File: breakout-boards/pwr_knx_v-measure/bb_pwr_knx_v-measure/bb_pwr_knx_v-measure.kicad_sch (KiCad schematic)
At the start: 47 parts, among them IC100 BD9G101, T1 BC856, T2 BCP52, T3 BC847

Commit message: bump bb_pwr_knx_v WIP
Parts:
- removed JP3: PINHD-1X2, bb_pwr_knx_v-measure:1X02, symbol bb_pwr_knx_v-measure-eagle-import:PINHD-1X2
- added C7: 100n, Capacitor_SMD:C_0805_2012Metric, symbol Device:C
- added D8: 1N4148W, Diode_SMD:D_SOD-123, symbol Diode:1N4148W
- added R14: 390k, Resistor_SMD:R_0805_2012Metric, symbol Device:R
- added R15: 43k, Resistor_SMD:R_0805_2012Metric, symbol Device:R
- C1: value 100uF 35V -> 100µ/35V; footprint bb_pwr_knx_v-measure:SANYO-OSCON_SMD_C6 -> Capacitor_SMD:CP_Elec_6.3x7.7; symbol bb_pwr_knx_v-measure-eagle-import:CPOL-EUSANYO_SMD_C6 -> Device:C_Polarized
- C10, C104, C2, C6: value 100nF -> 100n; footprint bb_pwr_knx_v-measure:C0805 -> Capacitor_SMD:C_0805_2012Metric; symbol bb_pwr_knx_v-measure-eagle-import:C-EUC0805 -> Device:C
- C100: value 4.7uF 50V -> 4.7µ/35V; footprint bb_pwr_knx_v-measure:C0805 -> Capacitor_SMD:C_0805_2012Metric; symbol bb_pwr_knx_v-measure-eagle-import:C-EUC0805 -> Device:C; REICHELT X7R-G1206 4,7/50 -> (none)
- C101: value 470nF -> 270n; footprint bb_pwr_knx_v-measure:C0805 -> Capacitor_SMD:C_0805_2012Metric; symbol bb_pwr_knx_v-measure-eagle-import:C-EUC0805 -> Device:C; now not fitted
- C102: value 15nF -> 15n; footprint bb_pwr_knx_v-measure:C0805 -> Capacitor_SMD:C_0805_2012Metric; symbol bb_pwr_knx_v-measure-eagle-import:C-EUC0805 -> Device:C; REICHELT X7R-G0805 15N -> (none)
- C103, C105: value 47uF 10V -> 47µ/10V; footprint bb_pwr_knx_v-measure:C0805 -> Capacitor_SMD:C_1206_3216Metric; symbol bb_pwr_knx_v-measure-eagle-import:C-EUC0805 -> Device:C
- C3, C4: value 10nF -> 10n; footprint bb_pwr_knx_v-measure:C0805 -> Capacitor_SMD:C_0805_2012Metric; symbol bb_pwr_knx_v-measure-eagle-import:C-EUC0805 -> Device:C
- C5: value 100pF -> 100p; footprint bb_pwr_knx_v-measure:C0805 -> Capacitor_SMD:C_0805_2012Metric; symbol bb_pwr_knx_v-measure-eagle-import:C-EUC0805 -> Device:C
- D1: value SMAJCA -> SMAJ40CA; footprint bb_pwr_knx_v-measure:DO214AC -> Diode_SMD:D_SMA; symbol bb_pwr_knx_v-measure-eagle-import:SMAJCA -> Diode:SMAJ40CA
- D100: value MBRS1100 -> RB060M-60 / MBR 140SFT1G; footprint bb_pwr_knx_v-measure:SOD-123 -> Diode_SMD:D_SOD-123; symbol bb_pwr_knx_v-measure-eagle-import:DIODESOD-123 -> Device:D_Schottky
- D2, D3, D4, D5: value 1N4148 -> 1N4148W; footprint bb_pwr_knx_v-measure:SOD-123 -> Diode_SMD:D_SOD-123; symbol bb_pwr_knx_v-measure-eagle-import:DIODESOD-123 -> Diode:1N4148W
- D6: footprint bb_pwr_knx_v-measure:SOD-123 -> Diode_SMD:D_SOD-123; symbol bb_pwr_knx_v-measure-eagle-import:DIODESOD-123 -> Device:D_Zener
- D7: value DDZ9685 -> 3V6; footprint bb_pwr_knx_v-measure:SOD-123 -> Diode_SMD:D_SOD-123; symbol bb_pwr_knx_v-measure-eagle-import:DIODESOD-123 -> Device:D_Zener
- IC100: value BD9G101 -> TPS560430; footprint bb_pwr_knx_v-measure:SOT23-6 -> Package_TO_SOT_SMD:SOT-23-6; symbol bb_pwr_knx_v-measure-eagle-import:BD9G101GBD9G101G-SOT23-6 -> Regulator_Switching:MCP16331x-xCH
- JP2: value PINHD-1X3 -> Conn_01x03_Pin; footprint bb_pwr_knx_v-measure:1X03 -> Connector_PinHeader_2.54mm:PinHeader_1x05_P2.54mm_Vertical; symbol bb_pwr_knx_v-measure-eagle-import:PINHD-1X3 -> Connector:Conn_01x05_Pin
- JP4: value PINHD-1X2 -> Conn_01x02_Pin; footprint bb_pwr_knx_v-measure:1X02 -> Connector_PinHeader_2.54mm:PinHeader_1x02_P2.54mm_Vertical; symbol bb_pwr_knx_v-measure-eagle-import:PINHD-1X2 -> Connector:Conn_01x02_Pin
- KNX0: footprint bb_pwr_knx_v-measure:WAGO-243-211 -> selfbus:W243-211_1x02_P5.75; symbol bb_pwr_knx_v-measure-eagle-import:WAGO-243-211 -> Connector:Screw_Terminal_01x02
- L1: footprint bb_pwr_knx_v-measure:BS11 -> selfbus:BS11_LIEGEND; SPICEPREFIX L -> (none)
- L100: value 4.7uH -> 10u; footprint bb_pwr_knx_v-measure:L4532P -> Inductor_SMD:L_1812_4532Metric; symbol bb_pwr_knx_v-measure-eagle-import:L-EUL4532P -> Device:L
- R1, R10, R11, R12, R13, R2, R3, R4, R5, R7, R8, R9: footprint bb_pwr_knx_v-measure:R0805 -> Resistor_SMD:R_0805_2012Metric; symbol bb_pwr_knx_v-measure-eagle-import:R-EU_R0805 -> Device:R
- R101: value 1k6 -> 88k7; footprint bb_pwr_knx_v-measure:R0805 -> Resistor_SMD:R_0805_2012Metric; symbol bb_pwr_knx_v-measure-eagle-import:R-EU_R0805 -> Device:R
- R102: value 470R -> 22k1; footprint bb_pwr_knx_v-measure:R0805 -> Resistor_SMD:R_0805_2012Metric; symbol bb_pwr_knx_v-measure-eagle-import:R-EU_R0805 -> Device:R
- R25: value 24R 2512 1.0W -> 24R 1W; footprint bb_pwr_knx_v-measure:R2512 -> Resistor_SMD:R_1206_3216Metric; symbol bb_pwr_knx_v-measure-eagle-import:R-EU_R2512 -> Device:R
- R6: footprint bb_pwr_knx_v-measure:R0805 -> Resistor_SMD:R_0805_2012Metric; symbol bb_pwr_knx_v-measure-eagle-import:R-EU_R0805 -> Device:R; REICHELT SMD-0805 5,60K -> (none)
- T1: footprint bb_pwr_knx_v-measure:SOT23-BEC -> Package_TO_SOT_SMD:SOT-23; symbol bb_pwr_knx_v-measure-eagle-import:BC856SMD -> Transistor_BJT:BC856
- T2: value BCP52 -> FZT753; footprint bb_pwr_knx_v-measure:SOT223 -> Package_TO_SOT_SMD:SOT-223-3_TabPin2; symbol bb_pwr_knx_v-measure-eagle-import:FZT753SMD -> Device:Q_PNP_BCE
- T3: footprint bb_pwr_knx_v-measure:SOT23 -> Package_TO_SOT_SMD:SOT-23; symbol bb_pwr_knx_v-measure-eagle-import:BC847 -> Transistor_BJT:BC847; REICHELT BC 847C SMD -> (none)
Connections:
- net +3V3: now also JP2.2 (Pin_2), D8.2 (A)
- net BUS_V: now also D7.1 (K), JP2.4 (Pin_4); no longer D7.C, JP2.2
- net EIB+: now also D1.2 (A2), D2.2 (A), D3.2 (A), KNX0.2 (Pin_2); no longer D1.C (2), D2.A, D3.A, KNX0.1+
- net EIB+DIR: now also D2.1 (K); no longer D2.C
- net EIB_DC: now also C1.1, D6.1 (K), C7.1, R14.2; no longer C1.+, D4.C, D6.C, IC100.4 (EN)
- net EIB_IN: now also C6.1, T1.2 (E); no longer T1.E
- net EIB_OUT: now also JP2.5 (Pin_5); no longer JP2.1
- net GND: now also C1.2, D1.1 (A1), D100.2 (A), D4.2 (A), D7.2 (A), JP2.1 (Pin_1), KNX0.1 (Pin_1), T1.3 (C), C7.2, R15.1; no longer C1.-, C6.1, D1.A (1), D100.A, D7.A, KNX0.2-, T1.C
- net N$8: no longer T2.4 (C)
- net REF: now also D5.2 (A), D6.2 (A); no longer D5.A, D6.A
- net at L1.2: now also D3.1 (K), D4.1 (K); no longer D3.C
- net at C102.1, IC100.6 (SW), L100.1: now also D100.1 (K); no longer D100.C
- net at C102.2, IC100.1 (BOOST): now also D8.1 (K)
- net at C2.2, R10.1: no longer D4.A
- net at R3.1, R4.2: now also D5.1 (K); no longer D5.C
- net at C2.1, R8.1, R9.2: now also T1.1 (B); no longer T1.B
- new net: IC100.4 (EN), R14.1, R15.2
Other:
- note added: "für Rohm BD9G101: R22=4k4, R23=680, C16=270n, D7 nicht bestücken für MCP16331: R22=31,25k, R23=10k, C16 nicht bestücken, D7 bestücken für TPS560430: R22=88,7k, R23=22,1k, C16 nicht bestücken, D7 nicht bestücken"
- note removed: "C101=4,7k/R101*0,15µF"
- note removed: "R101+R102<=Vo*1000"
- note removed: "R101=((Vo*R102)/0,75)-R102"
- note removed: "Rechnerische Werte R101: 1598R R102: 470R"
- note removed: "Rechnerischer Wert C101: ca. 440nF"
- moved on the sheet: JP4, KNX0

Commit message: bb_pwr_knx_v-measure final
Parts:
- renumbered C101 to C11, C104 to C12, C103 to C13, C105 to C14, C100 to C7, C7 to C8, C102 to C9, D100 to D9, IC100 to IC1, L100 to L2, R101 to R16, R102 to R17
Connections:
- net N$8 renamed HEAT
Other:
- moved on the sheet: C1, C10, C11, C12, C13, C14, C2, C3, C4, C5, C6, C7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

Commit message: finally standardize selected parts on all boards
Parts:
- D6, D7: footprint Diode_SMD:D_SOD-123 -> Diode_SMD:D_MiniMELF
- R13: value 6,2k -> 6k2
- R25: value 24R 1W -> 24R 1W
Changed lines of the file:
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@@
 			)
 		)
-		(property "Value" "24R  1W"
+		(property "Value" "24R 1W"
 			(at 65.278 171.7422 0)
 			(effects
@@
 			)
 		)
-		(property "Value" "6,2k"
+		(property "Value" "6k2"
 			(at 103.632 145.0722 0)
 			(effects
@@
 			)
 		)
-		(property "Footprint" "Diode_SMD:D_SOD-123"
+		(property "Footprint" "Diode_SMD:D_MiniMELF"
 			(at 86.36 130.81 0)
 			(effects
@@
 			)
 		)
-		(property "Footprint" "Diode_SMD:D_SOD-123"
+		(property "Footprint" "Diode_SMD:D_MiniMELF"
 			(at 113.03 143.51 0)
 			(effects

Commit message: final for manufacturing
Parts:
- C1: value 100µ/35V -> 100u/35V
- C13, C14: value 47µ/10V -> 47u/10V
- C7: value 4.7µ/35V -> 4.7u/35V
- R16: value 88k7 -> 51k
- R25: footprint Resistor_SMD:R_1206_3216Metric -> Resistor_SMD:R_2512_6332Metric
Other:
- note added: "für Rohm BD9G101: R22=4k4, R23=680, C16=270n, D7 nicht bestücken für MCP16331: R22=31,25k, R23=10k, C16 nicht bestücken, D7 bestücken für TPS560430: R22=51k, R23=22,1k, C16 nicht bestücken, D7 nicht bestücken"
- note removed: "für Rohm BD9G101: R22=4k4, R23=680, C16=270n, D7 nicht bestücken für MCP16331: R22=31,25k, R23=10k, C16 nicht bestücken, D7 bestücken für TPS560430: R22=88,7k, R23=22,1k, C16 nicht bestücken, D7 nicht bestücken"
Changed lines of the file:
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@@
 		)
 	)
-	(text "für Rohm BD9G101:\nR22=4k4, R23=680, C16=270n, D7 nicht bestücken\nfür MCP16331:\nR22=31,25k, R23=10k, C16 nicht bestücken, D7 bestücken\nfür TPS560430:\nR22=88,7k, R23=22,1k, C16 nicht bestücken, D7 nicht bestücken"
+	(text "für Rohm BD9G101:\nR22=4k4, R23=680, C16=270n, D7 nicht bestücken\nfür MCP16331:\nR22=31,25k, R23=10k, C16 nicht bestücken, D7 bestücken\nfür TPS560430:\nR22=51k, R23=22,1k, C16 nicht bestücken, D7 nicht bestücken"
 		(exclude_from_sim no)
 		(at 38.354 18.288 0)
@@
 			)
 		)
-		(property "Footprint" "Resistor_SMD:R_1206_3216Metric"
+		(property "Footprint" "Resistor_SMD:R_2512_6332Metric"
 			(at 65.278 170.18 90)
 			(effects
@@
 			)
 		)
-		(property "Value" "4.7µ/35V"
+		(property "Value" "4.7u/35V"
 			(at 20.32 57.785 0)
 			(effects
@@
 			)
 		)
-		(property "Value" "47µ/10V"
+		(property "Value" "47u/10V"
 			(at 154.94 57.785 0)
 			(effects
@@
 		(fields_autoplaced yes)
 		(property "Reference" "R16"
-			(at 111.76 48.895 0)
+			(at 110.998 49.2378 0)
 			(effects
 				(font
@@
 			)
 		)
-		(property "Value" "88k7"
-			(at 111.76 52.705 0)
+		(property "Value" "51k"
+			(at 110.998 52.3622 0)
 			(effects
 				(font
@@
 			)
 		)
-		(property "Value" "100µ/35V"
+		(property "Value" "100u/35V"
 			(at 68.961 89.5732 0)
 			(effects
@@
 			)
 		)
-		(property "Value" "47µ/10V"
+		(property "Value" "47u/10V"
 			(at 142.24 57.785 0)
 			(effects

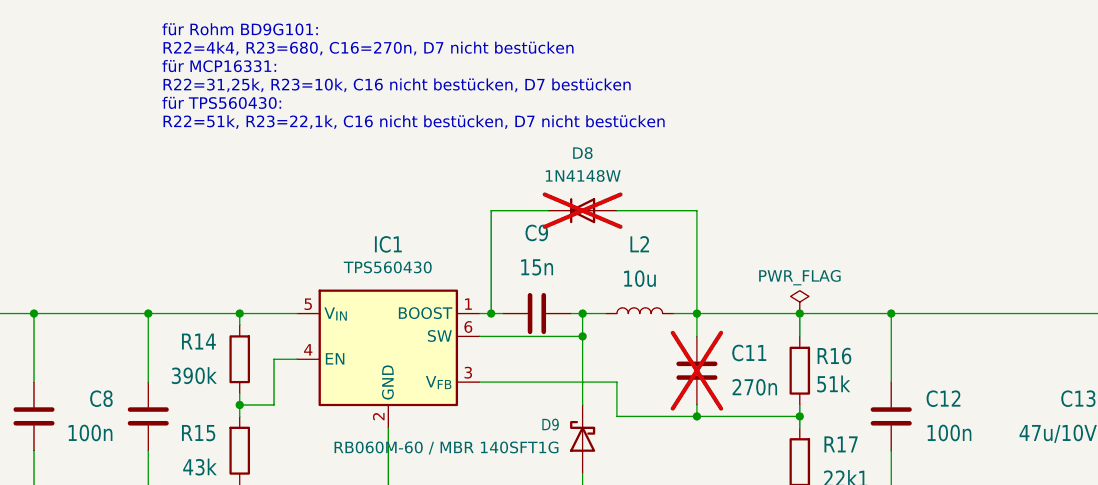
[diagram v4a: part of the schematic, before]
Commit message: update bb_pwr_knx_v-measure
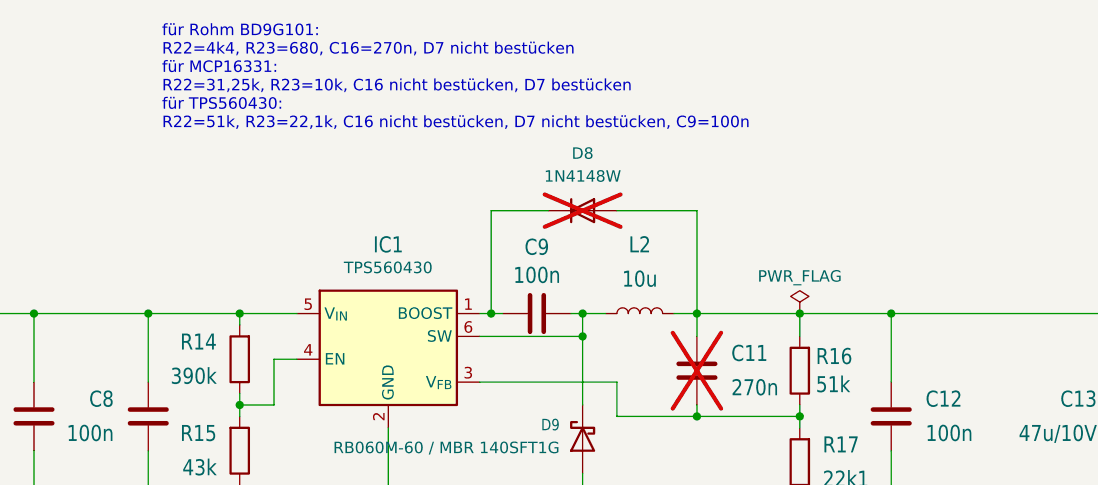
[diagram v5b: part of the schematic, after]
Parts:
- C9: value 15n -> 100n
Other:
- note added: "für Rohm BD9G101: R22=4k4, R23=680, C16=270n, D7 nicht bestücken für MCP16331: R22=31,25k, R23=10k, C16 nicht bestücken, D7 bestücken für TPS560430: R22=51k, R23=22,1k, C16 nicht bestücken, D7 nicht bestücken, C9=100n"
- note removed: "für Rohm BD9G101: R22=4k4, R23=680, C16=270n, D7 nicht bestücken für MCP16331: R22=31,25k, R23=10k, C16 nicht bestücken, D7 bestücken für TPS560430: R22=51k, R23=22,1k, C16 nicht bestücken, D7 nicht bestücken"
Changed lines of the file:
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@@
 		)
 	)
-	(text "für Rohm BD9G101:\nR22=4k4, R23=680, C16=270n, D7 nicht bestücken\nfür MCP16331:\nR22=31,25k, R23=10k, C16 nicht bestücken, D7 bestücken\nfür TPS560430:\nR22=51k, R23=22,1k, C16 nicht bestücken, D7 nicht bestücken"
+	(text "für Rohm BD9G101:\nR22=4k4, R23=680, C16=270n, D7 nicht bestücken\nfür MCP16331:\nR22=31,25k, R23=10k, C16 nicht bestücken, D7 bestücken\nfür TPS560430:\nR22=51k, R23=22,1k, C16 nicht bestücken, D7 nicht bestücken, C9=100n"
 		(exclude_from_sim no)
 		(at 38.354 18.288 0)
@@
 		(fields_autoplaced yes)
 		(property "Reference" "C9"
-			(at 80.01 35.56 90)
-			(effects
-				(font
-					(size 1.778 1.5113)
-				)
-			)
-		)
-		(property "Value" "15n"
-			(at 80.01 39.37 90)
-			(effects
-				(font
+			(at 80.01 37.0964 90)
+			(effects
+				(font
+					(size 1.778 1.5113)
+				)
+			)
+		)
+		(property "Value" "100n"
+			(at 80.01 40.2208 90)
+			(effects
+				(font

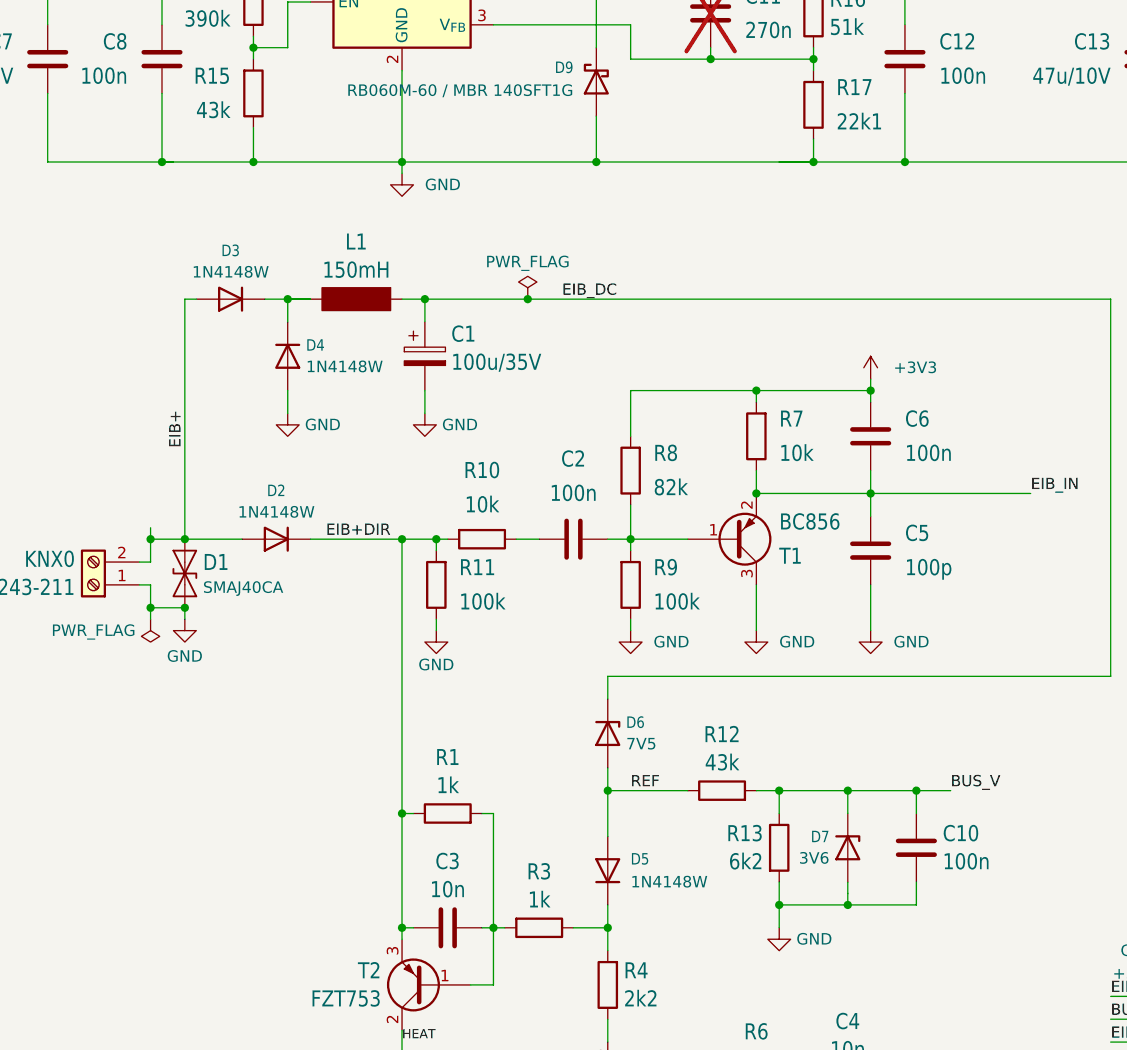
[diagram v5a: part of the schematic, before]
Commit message: update xtal caps, eib_in cap+resistor, bus_v resistors
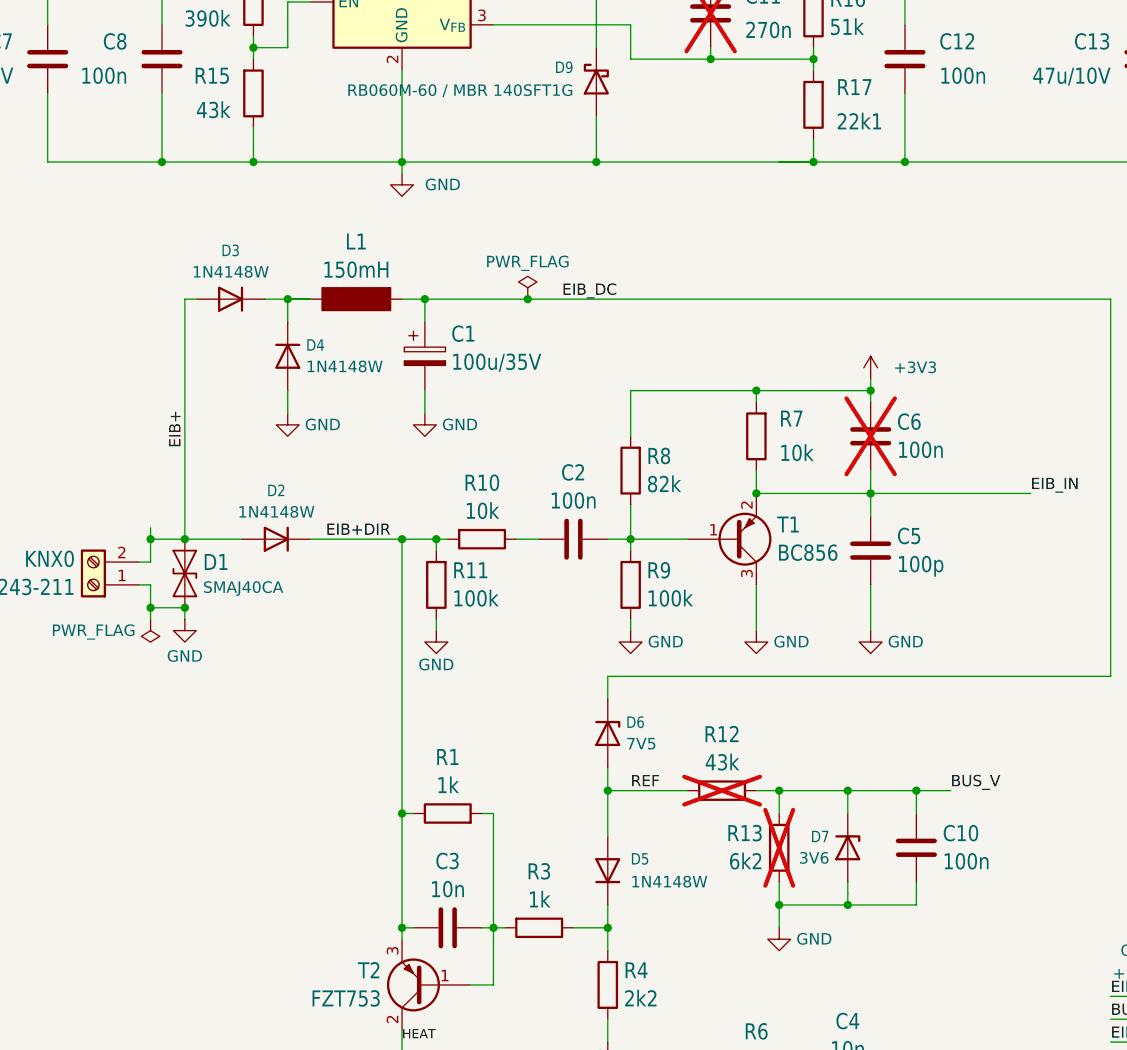
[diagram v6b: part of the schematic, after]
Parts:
- C6, R12, R13: now not fitted; now left out of the parts list
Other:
- moved on the sheet: R9
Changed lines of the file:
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@@
 	(wire
 		(pts
-			(xy 36.83 67.31) (xy 38.1 67.31)
-		)
-		(stroke
-			(width 0)
-			(type default)
-		)
-	)
-	(wire
-		(pts
 			(xy 151.13 157.48) (xy 157.48 157.48)
 		)
@@
 		(unit 1)
 		(exclude_from_sim no)
-		(in_bom yes)
+		(in_bom no)
 		(on_board yes)
-		(dnp no)
+		(dnp yes)
 		(fields_autoplaced yes)
 		(property "Reference" "C6"
-			(at 119.38 95.885 0)
+			(at 118.491 96.2278 0)
 			(effects
 				(font
@@
 		)
 		(property "Value" "100n"
-			(at 119.38 99.695 0)
+			(at 118.491 99.3522 0)
 			(effects
 				(font
@@
 		(on_board yes)
 		(dnp no)
+		(fields_autoplaced yes)
 		(property "Reference" "R11"
-			(at 69.85 112.395 0)
+			(at 69.088 112.7378 0)
 			(effects
 				(font
@@
 		)
 		(property "Value" "100k"
-			(at 69.85 116.205 0)
+			(at 69.088 115.8622 0)
 			(effects
 				(font
@@
 		(fields_autoplaced yes)
 		(property "Reference" "R10"
-			(at 72.39 101.6 90)
+			(at 72.39 103.0094 90)
 			(effects
 				(font
@@
 		)
 		(property "Value" "10k"
-			(at 72.39 105.41 90)
+			(at 72.39 106.1338 90)
 			(effects
 				(font
@@
 		)
 		(property "Value" "GND"
-			(at 118.11 120.6499 0)
+			(at 117.475 120.65 0)
 			(effects
 				(font
@@
 		(unit 1)
 		(exclude_from_sim no)
-		(in_bom yes)
+		(in_bom no)
 		(on_board yes)
-		(dnp no)
+		(dnp yes)
 		(fields_autoplaced yes)
 		(property "Reference" "R13"
@@
 		(fields_autoplaced yes)
 		(property "Reference" "R8"
-			(at 91.44 99.695 0)
+			(at 90.678 100.0378 0)
 			(effects
 				(font
@@
 		)
 		(property "Value" "82k"
-			(at 91.44 103.505 0)
+			(at 90.678 103.1622 0)
 			(effects
 				(font
@@
 		)
 		(property "Value" "GND"
-			(at 105.41 120.6499 0)
+			(at 104.775 120.65 0)
 			(effects
 				(font
@@
 	(symbol
 		(lib_id "Device:R")
-		(at 88.9 114.3 0)
-		(mirror x)
+		(at 88.9 114.3 180)
 		(unit 1)
 		(exclude_from_sim no)
@@
 		(dnp no)
 		(property "Reference" "R9"
-			(at 91.44 112.395 0)
+			(at 90.678 112.7378 0)
 			(effects
 				(font
 					(size 1.778 1.5113)
 				)
-				(justify left)
+				(justify right)
 			)
 		)
 		(property "Value" "100k"
-			(at 91.44 116.205 0)
+			(at 90.678 115.8622 0)
 			(effects
 				(font
 					(size 1.778 1.5113)
 				)
-				(justify left)
+				(justify right)
 			)
 		)
 		(property "Footprint" "Resistor_SMD:R_0805_2012Metric"
-			(at 87.122 114.3 90)
+			(at 90.678 114.3 90)
 			(effects
 				(font
@@
 		(unit 1)
 		(exclude_from_sim no)
-		(in_bom yes)
+		(in_bom no)
 		(on_board yes)
-		(dnp no)
+		(dnp yes)
 		(fields_autoplaced yes)
 		(property "Reference" "R12"
@@
 		(fields_autoplaced yes)
 		(property "Reference" "C5"
-			(at 119.38 108.585 0)
+			(at 118.491 108.9278 0)
 			(effects
 				(font
@@
 		)
 		(property "Value" "100p"
-			(at 119.38 112.395 0)
+			(at 118.491 112.0522 0)
 			(effects
 				(font
@@
 		(on_board yes)
 		(dnp no)
+		(fields_autoplaced yes)
 		(property "Reference" "T1"
-			(at 105.41 111.125 0)
+			(at 105.1814 107.6578 0)
 			(effects
 				(font
@@
 		)
 		(property "Value" "BC856"
-			(at 105.41 107.315 0)
+			(at 105.1814 110.7822 0)
 			(effects
 				(font
@@
 		)
 		(property "Value" "GND"
-			(at 91.44 120.6499 0)
+			(at 90.805 120.65 0)
 			(effects
 				(font
@@
 		(fields_autoplaced yes)
 		(property "Reference" "C2"
-			(at 82.55 100.33 90)
+			(at 82.55 101.8664 90)
 			(effects
 				(font
@@
 		)
 		(property "Value" "100n"
-			(at 82.55 104.14 90)
+			(at 82.55 104.9908 90)
 			(effects
 				(font
